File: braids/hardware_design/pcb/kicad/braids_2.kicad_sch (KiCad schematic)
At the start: 49 parts

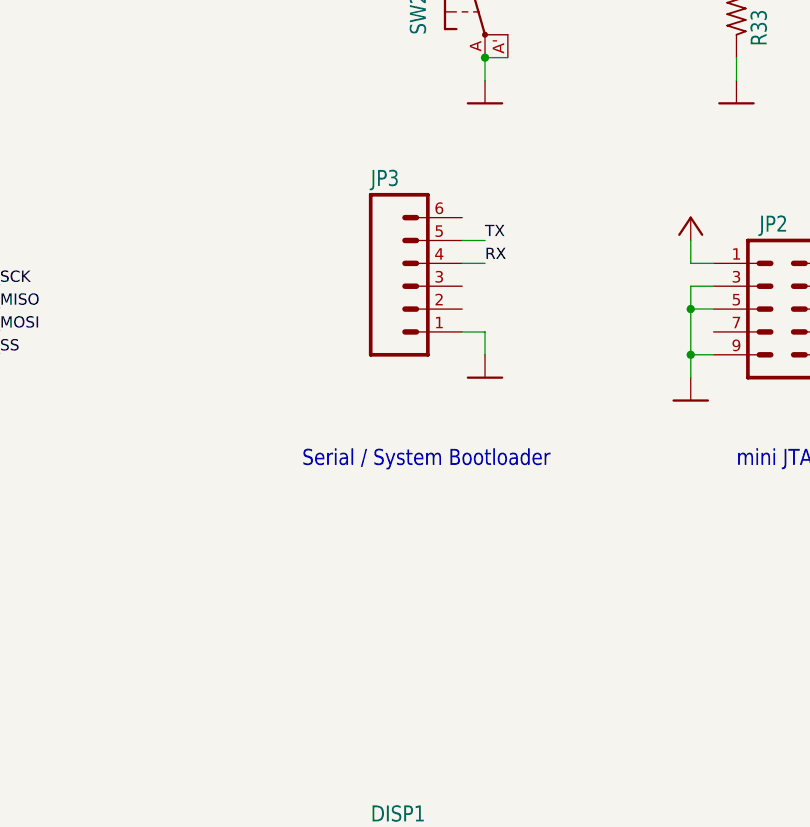
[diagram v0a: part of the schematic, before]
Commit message: add surfact mount serial flashing header
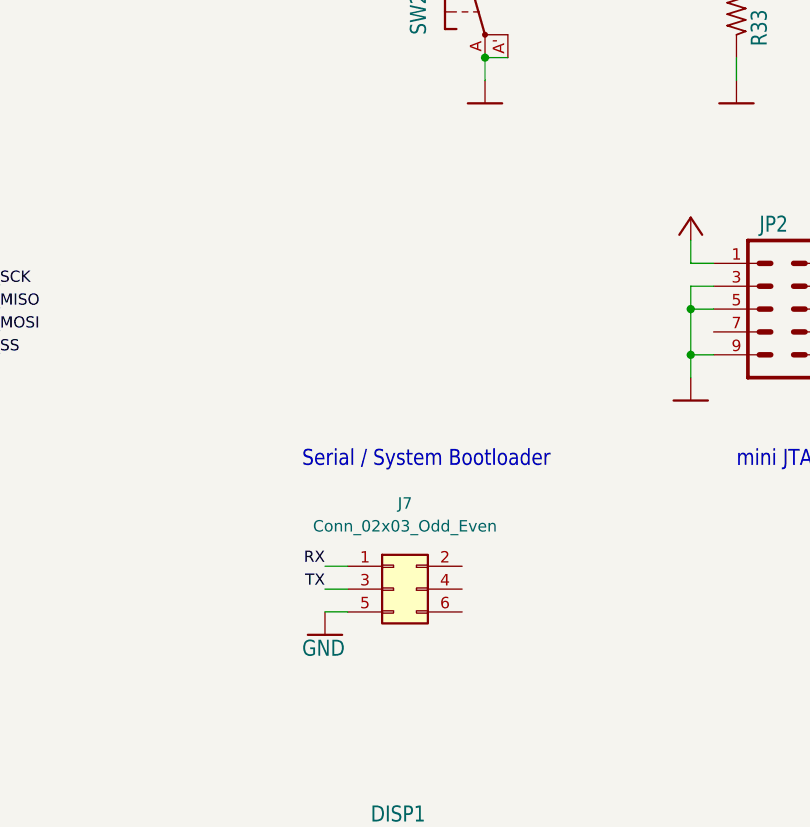
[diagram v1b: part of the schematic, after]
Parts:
- removed JP3: (no value), symbol braids-eagle-import:M06SIP
- added J7: Conn_02x03_Odd_Even, Connector_PinHeader_2.54mm:PinHeader_2x03_P2.54mm_Horizontal_SMD, symbol Connector_Generic:Conn_02x03_Odd_Even
- C1: footprint (none) -> Connector_PinHeader_2.54mm:PinHeader_2x03_P2.54mm_Horizontal_SMD
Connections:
- net GND: now also J7.5 (Pin_5)
- net RX: now also J7.1 (Pin_1)
- net TX: now also J7.3 (Pin_3)
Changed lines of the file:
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@@
-    (stroke (width 0) (type default) (color 0 0 0 0))
-  )
-  (wire (pts (xy 335.28 93.98) (xy 337.82 93.98))
     (stroke (width 0) (type default) (color 0 0 0 0))
   )
@@
     (stroke (width 0) (type default) (color 0 0 0 0))
   )
+  (wire (pts (xy 320.04 130.175) (xy 322.58 130.175))
+    (stroke (width 0) (type default) (color 0 0 0 0))
+  )
   (wire (pts (xy 220.98 180.34) (xy 243.84 180.34))
     (stroke (width 0) (type default) (color 0 0 0 0))
@@
     (stroke (width 0) (type default) (color 0 0 0 0))
   )
-  (wire (pts (xy 335.28 101.6) (xy 337.82 101.6))
-    (stroke (width 0) (type default) (color 0 0 0 0))
-  )
   (wire (pts (xy 358.14 210.82) (xy 360.68 210.82))
     (stroke (width 0) (type default) (color 0 0 0 0))
@@
     (stroke (width 0) (type default) (color 0 0 0 0))
   )
+  (wire (pts (xy 320.04 132.715) (xy 322.58 132.715))
+    (stroke (width 0) (type default) (color 0 0 0 0))
+  )
   (wire (pts (xy 121.92 116.84) (xy 127 116.84))
     (stroke (width 0) (type default) (color 0 0 0 0))
@@
     (stroke (width 0) (type default) (color 0 0 0 0))
   )
-  (wire (pts (xy 337.82 101.6) (xy 337.82 104.14))
-    (stroke (width 0) (type default) (color 0 0 0 0))
-  )
   (wire (pts (xy 261.62 162.56) (xy 322.58 162.56))
     (stroke (width 0) (type default) (color 0 0 0 0))
@@
     (stroke (width 0) (type default) (color 0 0 0 0))
   )
+  (wire (pts (xy 320.04 127.635) (xy 322.58 127.635))
+    (stroke (width 0) (type default) (color 0 0 0 0))
+  )
   (wire (pts (xy 101.6 256.54) (xy 109.22 256.54))
     (stroke (width 0) (type default) (color 0 0 0 0))
@@
   )
   (wire (pts (xy 73.66 60.96) (xy 60.96 60.96))
-    (stroke (width 0) (type default) (color 0 0 0 0))
-  )
-  (wire (pts (xy 335.28 91.44) (xy 337.82 91.44))
     (stroke (width 0) (type default) (color 0 0 0 0))
   )
@@
     (effects (font (size 1.2446 1.2446)) (justify right bottom))
   )
+  (label "RX" (at 320.04 127.635 180)
+    (effects (font (size 1.2446 1.2446)) (justify right bottom))
+  )
   (label "ADC_SS" (at 86.36 91.44 180)
     (effects (font (size 1.2446 1.2446)) (justify right bottom))
@@
     (effects (font (size 1.2446 1.2446)) (justify left bottom))
   )
-  (label "TX" (at 337.82 91.44 0)
-    (effects (font (size 1.2446 1.2446)) (justify left bottom))
-  )
   (label "DAC_SS" (at 243.84 58.42 180)
     (effects (font (size 1.2446 1.2446)) (justify right bottom))
@@
     (effects (font (size 1.2446 1.2446)) (justify right bottom))
   )
-  (label "RX" (at 337.82 93.98 0)
-    (effects (font (size 1.2446 1.2446)) (justify left bottom))
-  )
   (label "RESET" (at 86.36 68.58 180)
     (effects (font (size 1.2446 1.2446)) (justify right bottom))
@@
   )
   (label "ENC_B" (at 86.36 60.96 180)
+    (effects (font (size 1.2446 1.2446)) (justify right bottom))
+  )
+  (label "TX" (at 320.04 130.175 180)
     (effects (font (size 1.2446 1.2446)) (justify right bottom))
   )
@@
     (pin "2")
   )
-  (symbol (lib_id "braids-eagle-import:M06SIP") (at 330.2 96.52 0) (unit 1)
-    (in_bom yes) (on_board yes)
-    (property "Reference" "JP3" (id 0) (at 325.12 85.598 0)
-      (effects (font (size 1.778 1.5113)) (justify left bottom))
-    )
-    (property "Value" "" (id 1) (at 325.12 106.68 0)
-      (effects (font (size 1.778 1.5113)) (justify left bottom))
-    )
-    (property "Footprint" "" (id 2) (at 330.2 96.52 0)
-      (effects (font (size 1.27 1.27)) hide)
-    )
-    (property "Datasheet" "" (id 3) (at 330.2 96.52 0)
-      (effects (font (size 1.27 1.27)) hide)
-    )
-    (pin "1")
-    (pin "2")
-    (pin "3")
-    (pin "4")
-    (pin "5")
-    (pin "6")
-  )
   (symbol (lib_id "braids-eagle-import:GND") (at 317.5 220.98 0) (unit 1)
     (in_bom yes) (on_board yes)
@@
     (pin "8")
     (pin "9")
+  )
+  (symbol (lib_id "braids-eagle-import:GND") (at 320.04 135.255 0) (unit 1)
+    (in_bom yes) (on_board yes)
+    (property "Reference" "#GND0101" (id 0) (at 320.04 135.255 0)
+      (effects (font (size 1.27 1.27)) hide)
+    )
+    (property "Value" "GND" (id 1) (at 317.5 137.795 0)
+      (effects (font (size 1.778 1.5113)) (justify left bottom))
+    )
+    (property "Footprint" "braids:" (id 2) (at 320.04 135.255 0)
+      (effects (font (size 1.27 1.27)) hide)
+    )
+    (property "Datasheet" "" (id 3) (at 320.04 135.255 0)
+      (effects (font (size 1.27 1.27)) hide)
+    )
+    (pin "1")
   )
   (symbol (lib_id "braids-eagle-import:M05X2MINIJTAG") (at 370.84 99.06 0) (unit 1)
@@
       (effects (font (size 1.778 1.5113)) (justify left bottom))
     )
-    (property "Footprint" "" (id 2) (at 101.6 246.38 0)
+    (property "Footprint" "Connector_PinHeader_2.54mm:PinHeader_2x03_P2.54mm_Horizontal_SMD" (id 2) (at 101.6 246.38 0)
       (effects (font (size 1.27 1.27)) hide)
     )
@@
     (pin "1")
     (pin "2")
+  )
+  (symbol (lib_id "Connector_Generic:Conn_02x03_Odd_Even") (at 327.66 130.175 0) (unit 1)
+    (in_bom yes) (on_board yes) (fields_autoplaced)
+    (property "Reference" "J7" (id 0) (at 328.93 120.65 0))
+    (property "Value" "Conn_02x03_Odd_Even" (id 1) (at 328.93 123.19 0))
+    (property "Footprint" "Connector_PinHeader_2.54mm:PinHeader_2x03_P2.54mm_Horizontal_SMD" (id 2) (at 327.66 130.175 0)
+      (effects (font (size 1.27 1.27)) hide)
+    )
+    (property "Datasheet" "~" (id 3) (at 327.66 130.175 0)
+      (effects (font (size 1.27 1.27)) hide)
+    )
+    (pin "1")
+    (pin "2")
+    (pin "3")
+    (pin "4")
+    (pin "5")
+    (pin "6")
   )
   (symbol (lib_id "braids-eagle-import:POT_USVERTICAL_PS") (at 48.26 200.66 0) (unit 1)
@@
     (pin "2")
   )
-  (symbol (lib_id "braids-eagle-import:GND") (at 337.82 106.68 0) (unit 1)
-    (in_bom yes) (on_board yes)
-    (property "Reference" "#GND61" (id 0) (at 337.82 106.68 0)
-      (effects (font (size 1.27 1.27)) hide)
-    )
-    (property "Value" "" (id 1) (at 335.28 109.22 0)
-      (effects (font (size 1.778 1.5113)) (justify left bottom))
-    )
-    (property "Footprint" "" (id 2) (at 337.82 106.68 0)
-      (effects (font (size 1.27 1.27)) hide)
-    )
-    (property "Datasheet" "" (id 3) (at 337.82 106.68 0)
-      (effects (font (size 1.27 1.27)) hide)
-    )
-    (pin "1")
-  )
   (symbol (lib_id "braids-eagle-import:+3V3") (at 48.26 187.96 0) (unit 1)

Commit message: move new header
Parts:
- C1: footprint Connector_PinHeader_2.54mm:PinHeader_2x03_P2.54mm_Horizontal_SMD -> braids:C0603
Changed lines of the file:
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@@
       (effects (font (size 1.778 1.5113)) (justify left bottom))
     )
-    (property "Footprint" "Connector_PinHeader_2.54mm:PinHeader_2x03_P2.54mm_Horizontal_SMD" (id 2) (at 101.6 246.38 0)
+    (property "Footprint" "braids:C0603" (id 2) (at 101.6 246.38 0)
       (effects (font (size 1.27 1.27)) hide)
     )

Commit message: fix DRC
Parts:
- JP2: footprint (none) -> braids:AVR_ICSP
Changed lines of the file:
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@@
       (effects (font (size 1.778 1.5113)) (justify left bottom))
     )
-    (property "Footprint" "" (id 2) (at 370.84 99.06 0)
+    (property "Footprint" "braids:AVR_ICSP" (id 2) (at 370.84 99.06 0)
       (effects (font (size 1.27 1.27)) hide)
     )

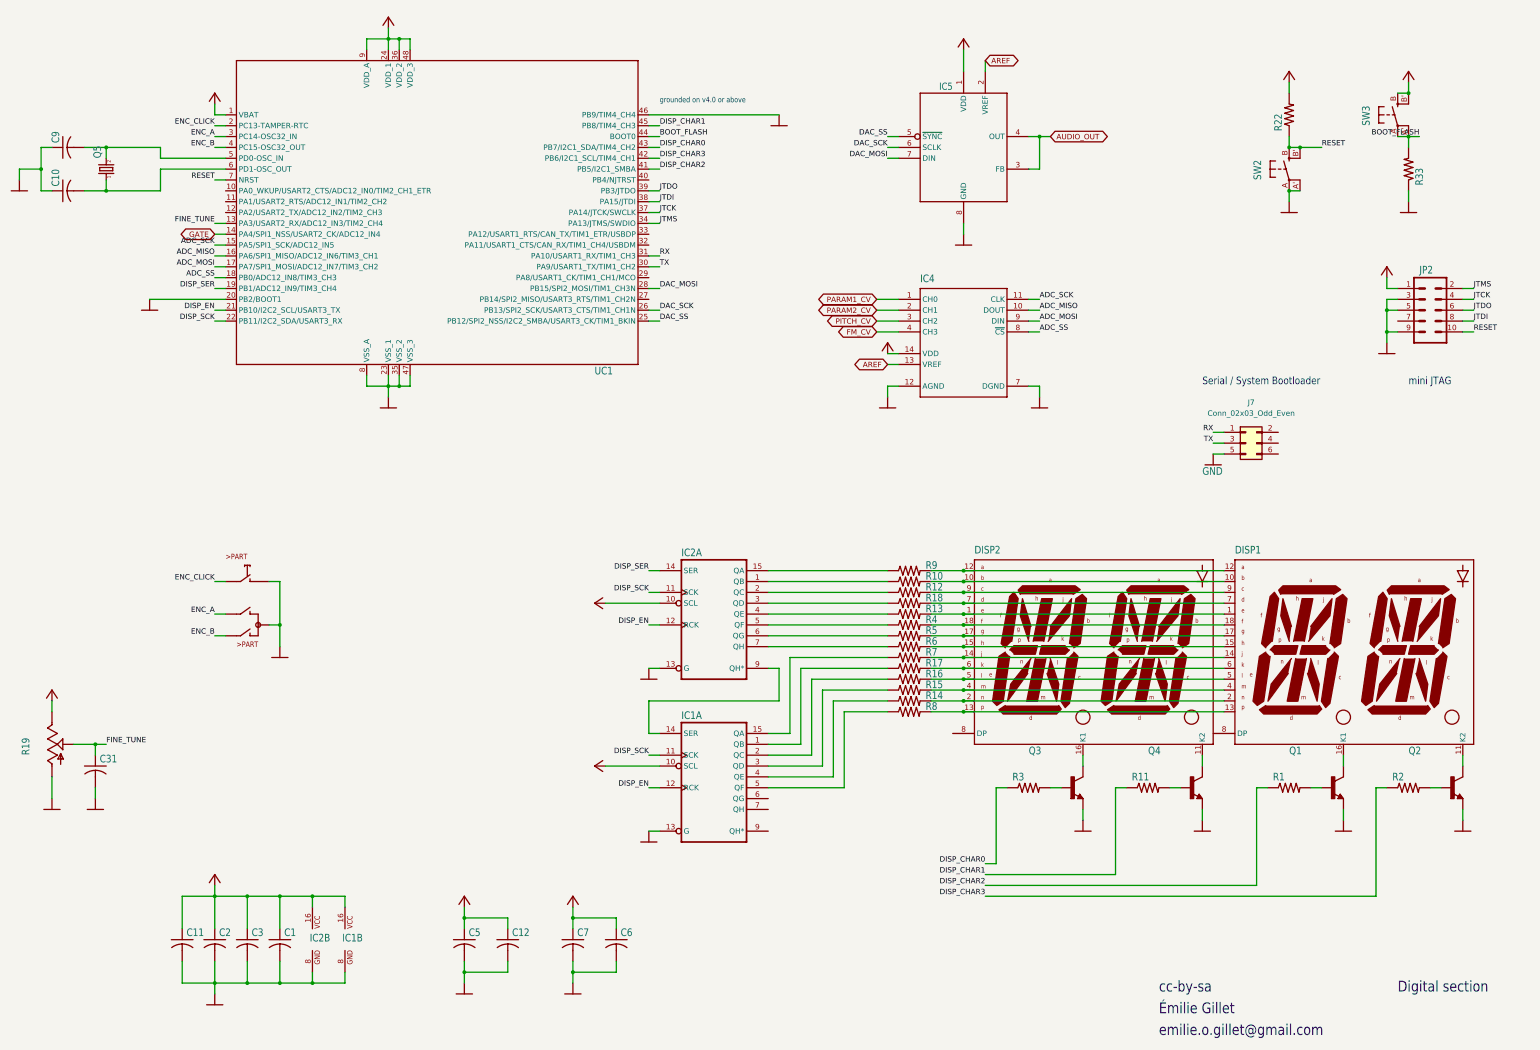
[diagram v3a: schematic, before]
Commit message: changed mcp3204 to mcp3208
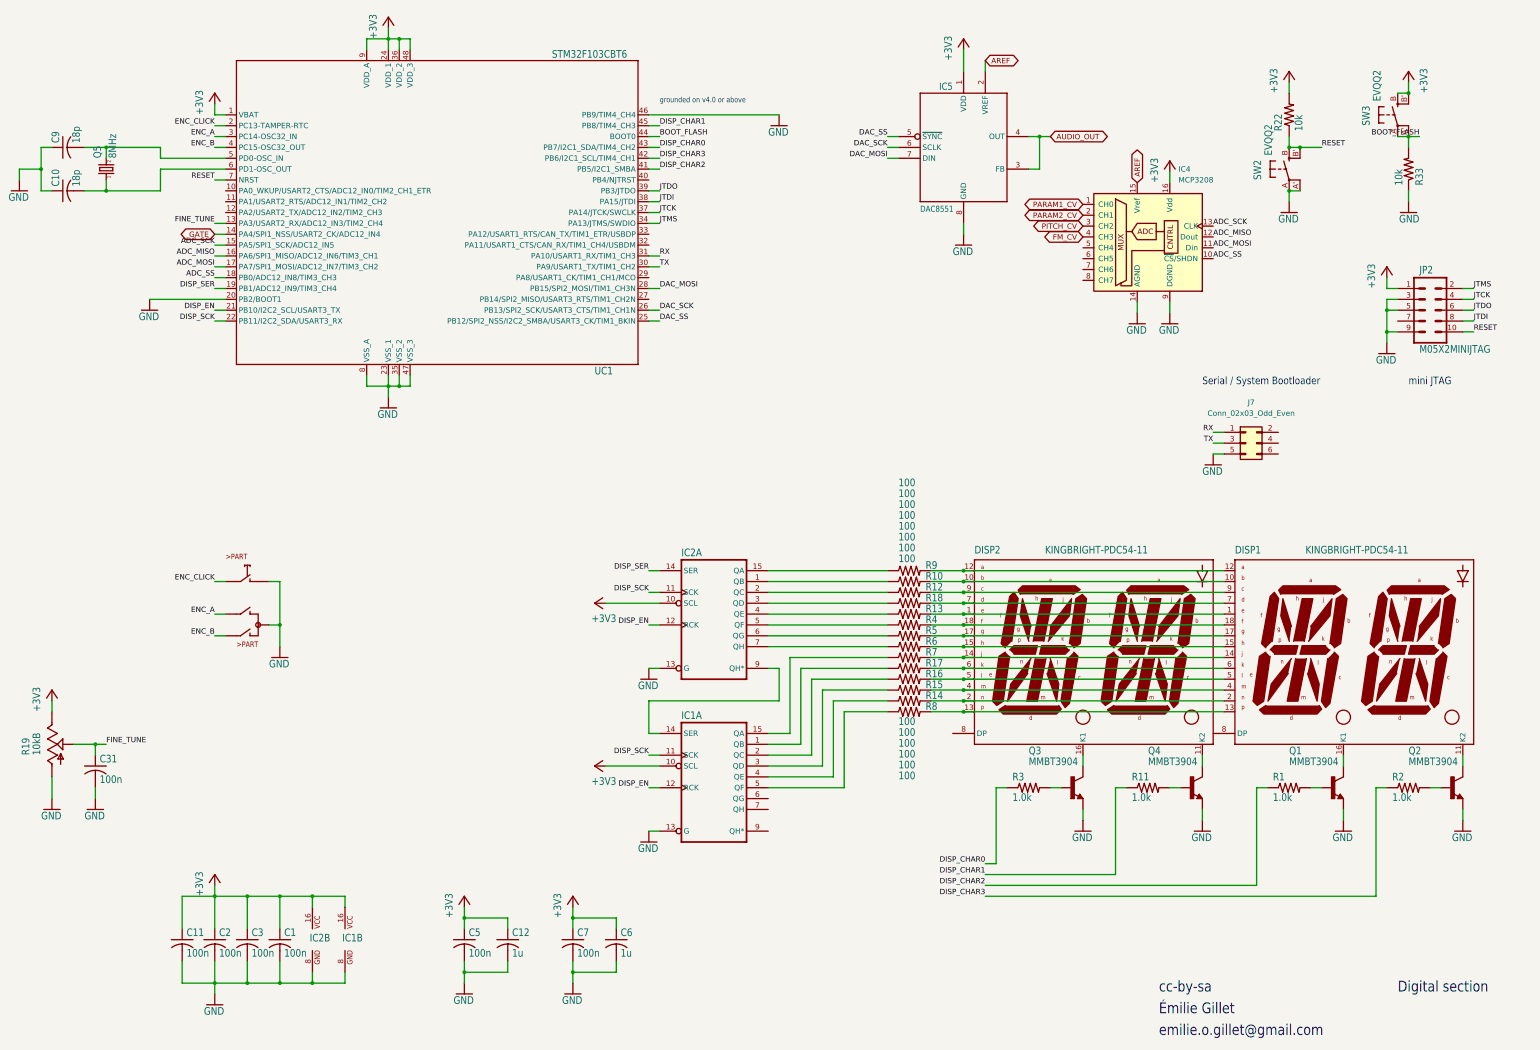
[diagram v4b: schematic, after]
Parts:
- removed IC4: (no value), symbol braids-eagle-import:MCP3302
- added IC4: MCP3208, Package_SO:SOIC-16_3.9x9.9mm_P1.27mm, symbol Analog_ADC:MCP3208
- C1: value (none) -> 100n
- C10, C9: value (none) -> 18p; footprint (none) -> braids:C0603
- C11, C2, C3, C31, C5, C7: value (none) -> 100n; footprint (none) -> braids:C0603
- C12, C6: value (none) -> 1u; footprint (none) -> braids:C0603
- DISP1, DISP2: value (none) -> KINGBRIGHT-PDC54-11; footprint (none) -> braids:PDC54
- IC1, IC2: value (none) -> 74595D; footprint (none) -> braids:SO16
- IC5: value (none) -> DAC8551; footprint (none) -> braids:MSOP-8
- JP2: value (none) -> M05X2MINIJTAG
- Q1, Q2, Q3, Q4: value (none) -> MMBT3904; footprint (none) -> braids:SOT23-BEC
- Q5: value (none) -> 8MHz; footprint (none) -> braids:HC49UP
- R1, R11, R2, R3: value (none) -> 1.0k; footprint (none) -> braids:R0603
- R10, R12, R13, R14, R15, R16, R17, R18, R4, R5, R6, R7, R8, R9: value (none) -> 100; footprint (none) -> braids:R0603
- R19: value (none) -> 10kB; footprint (none) -> braids:ALPS_POT_VERTICAL_PS
- R22, R33: value (none) -> 10k; footprint (none) -> braids:R0603
- SW1: value (none) -> EC12E_SW; footprint (none) -> braids:ALPS_EC12E_SW
- SW2, SW3: value (none) -> EVQQ2; footprint (none) -> braids:EVQ-Q2
- UC1: value (none) -> STM32F103CBT6; footprint (none) -> braids:LQFP48
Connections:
- net +3V3: now also IC4.16 (Vdd)
- net ADC_MISO: now also IC4.12 (Dout)
- net ADC_MOSI: now also IC4.11 (Din)
- net ADC_SCK: now also IC4.13 (CLK)
- net ADC_SS: now also IC4.10 (~{CS}/SHDN)
- net AREF: now also IC4.15 (Vref)
- net FM_CV: now also IC4.4 (CH3)
- net GND: now also IC4.14 (AGND), IC4.9 (DGND)
- net PARAM1_CV: now also IC4.1 (CH0)
- net PARAM2_CV: now also IC4.2 (CH1)
- net PITCH_CV: now also IC4.3 (CH2)
